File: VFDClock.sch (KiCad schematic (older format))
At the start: 24 parts, among them J1 Barrel_Jack_MountingPin, P1 Power, P2 Analog, P3 Digital, P4 Digital, Q1 VFD_LD8035E, Q2 VFD_LD8035E, Q3 VFD_LD8035E, Q4 VFD_LD8035E, Q5 VFD_LD8035E, Q6 VFD_LD8035E, U1 IC_HT16K33, U2 RTC_DS3231, U3 TBD62783APG, U4 TBD62783APG

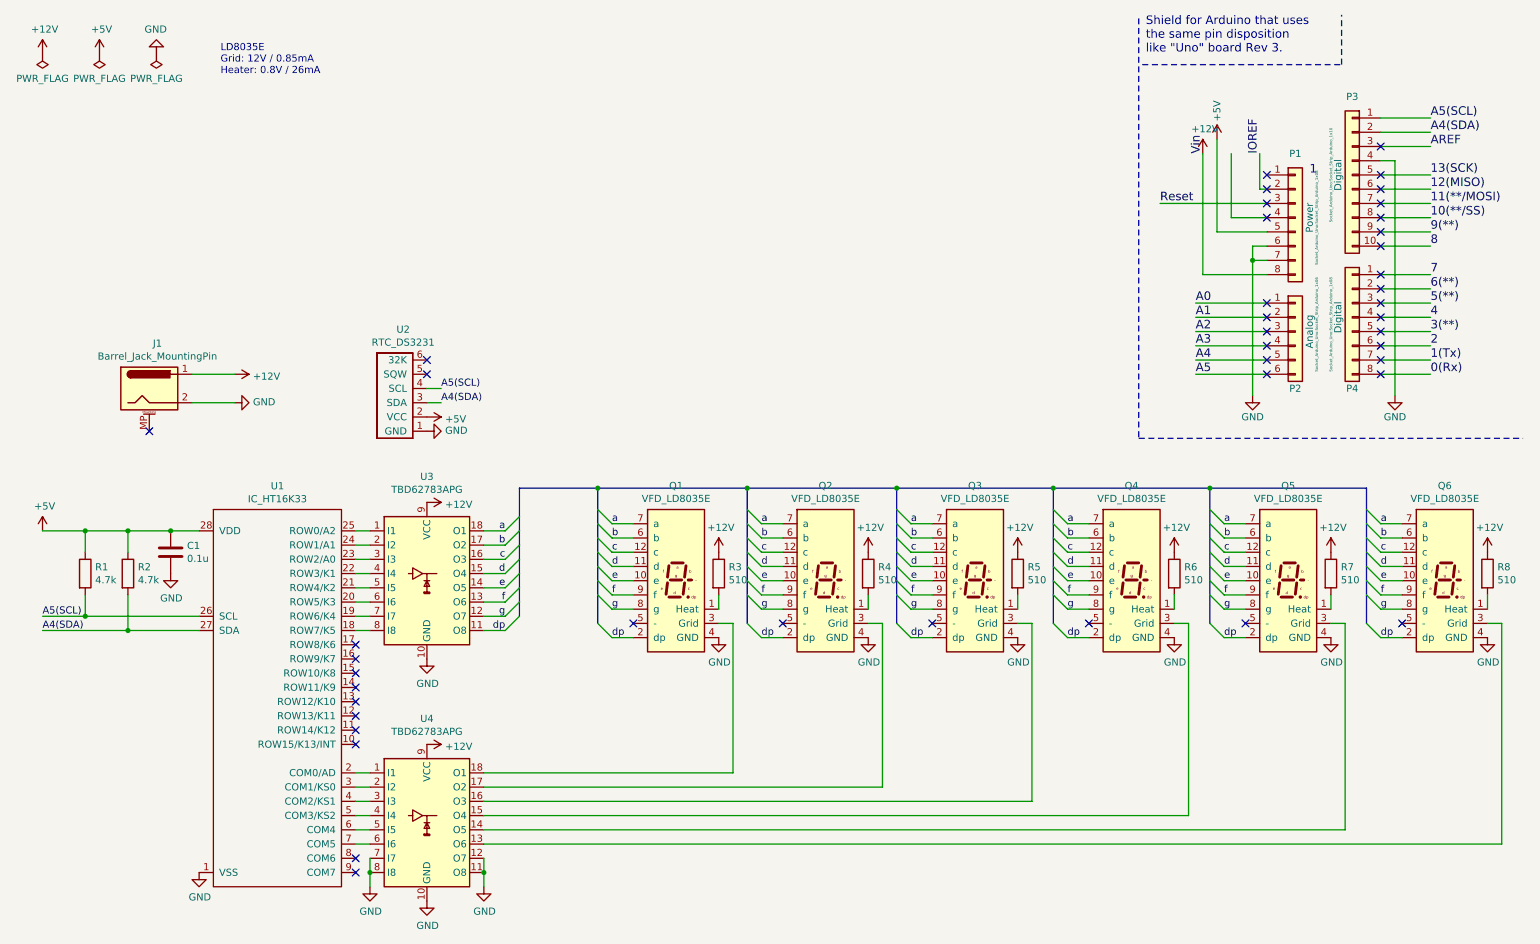
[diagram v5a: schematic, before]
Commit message: RTCを置き換え
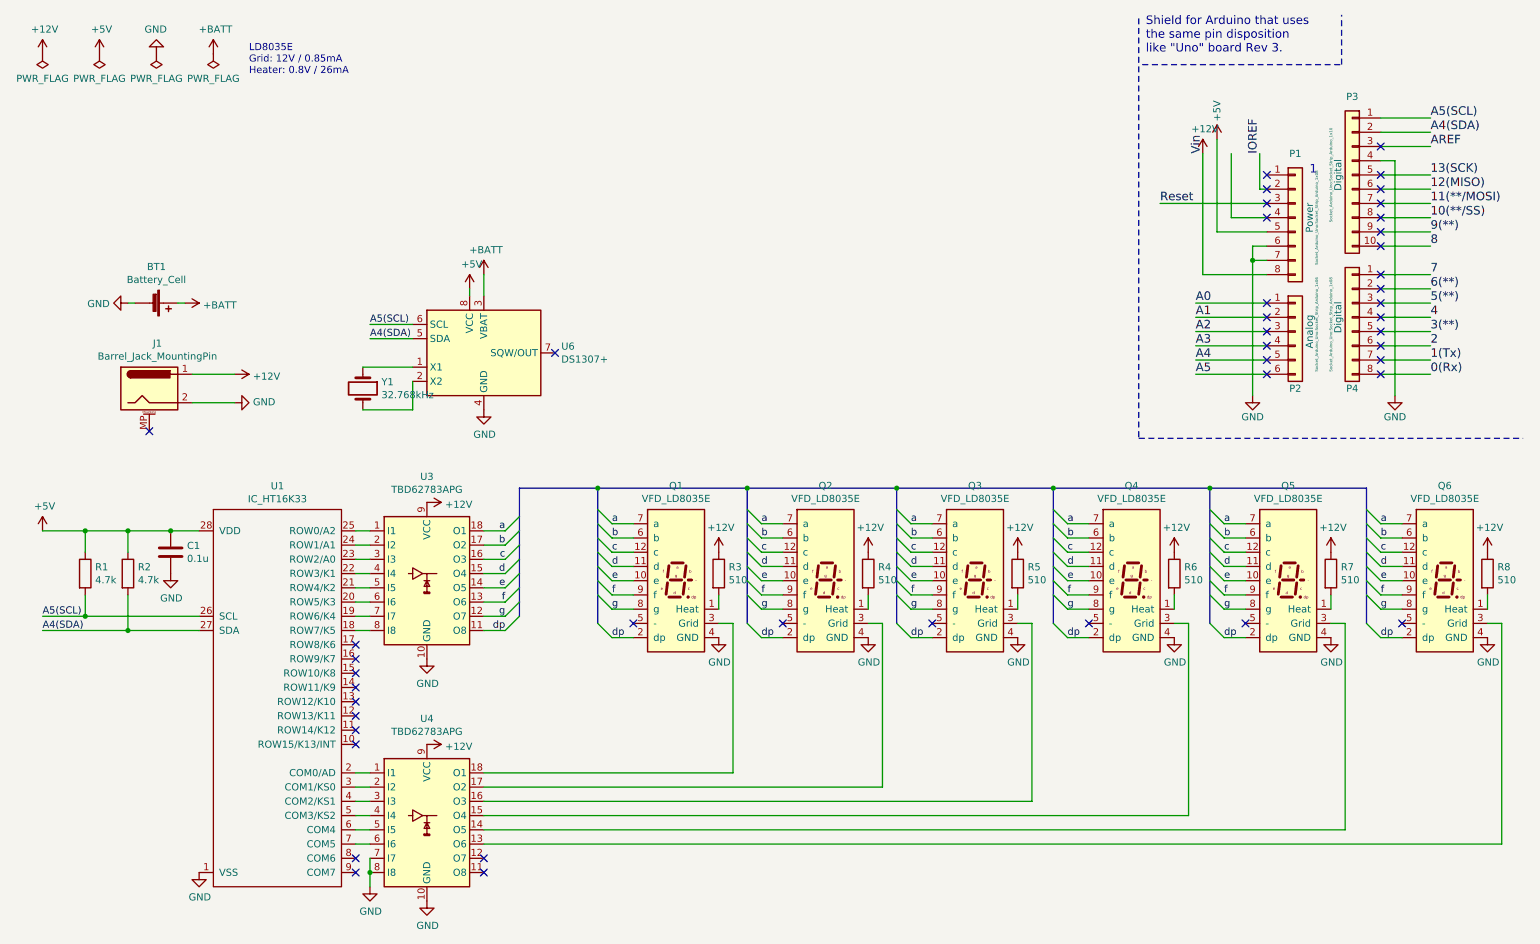
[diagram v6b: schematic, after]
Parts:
- removed U2: RTC_DS3231, #MyFootPrints:RTC_DS3231_Vertical, symbol MyParts:RTC_DS3231
- added BT1: Battery_Cell, symbol Device:Battery_Cell
- added U6: DS1307+, Package_DIP:DIP-8_W7.62mm, symbol Timer_RTC:DS1307+
- added Y1: 32.768kHz, symbol Device:Crystal
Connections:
- net +5V: now also U6.8 (VCC)
- net A4(SDA): now also U6.5 (SDA)
- net A5(SCL): now also U6.6 (SCL)
- net GND: now also BT1.2 (-), U6.4 (GND); no longer U4.11 (O8), U4.12 (O7)
- new net: U6.1 (X1), Y1.1
- new net: U6.2 (X2), Y1.2
- new net +BATT: BT1.1 (+), U6.3 (VBAT)
- no-connect marks 44 -> 45
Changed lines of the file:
@@
 NoConn ~ 9400 3000
-$Comp
-L MyParts:RTC_DS3231 U2
-U 1 1 5F2CBB77
-P 3350 3150
-F 0 "U2" V 3815 3167 50  0000 C CNN
-F 1 "RTC_DS3231" V 3724 3167 50  0000 C CNN
-F 2 "#MyFootPrints:RTC_DS3231_Vertical" H 3350 3500 50  0001 C CNN
-F 3 "" H 3350 3500 50  0001 C CNN
-	1    3350 3150
-	0    -1   -1   0
-$EndComp
-$Comp
-L power:GND #PWR0117
-U 1 1 5F2CDC62
-P 3500 3400
-F 0 "#PWR0117" H 3500 3150 50  0001 C CNN
-F 1 "GND" V 3505 3272 50  0000 R CNN
-F 2 "" H 3500 3400 50  0001 C CNN
-F 3 "" H 3500 3400 50  0001 C CNN
-	1    3500 3400
-	0    -1   -1   0
-$EndComp
-$Comp
-L power:+5V #PWR0118
-U 1 1 5F2CEAC2
-P 3500 3300
-F 0 "#PWR0118" H 3500 3150 50  0001 C CNN
-F 1 "+5V" V 3515 3428 50  0000 L CNN
-F 2 "" H 3500 3300 50  0001 C CNN
-F 3 "" H 3500 3300 50  0001 C CNN
-	1    3500 3300
-	0    1    1    0
-$EndComp
-Wire Wire Line
-	3500 3200 3600 3200
-Wire Wire Line
-	3500 3100 3600 3100
-NoConn ~ 3500 3000
-NoConn ~ 3500 2900
-Text Label 3600 3200 0    50   ~ 0
-A4(SDA)
-Text Label 3600 3100 0    50   ~ 0
-A5(SCL)
 $Comp
 L Transistor_Array:TBD62783A U3
@@
 	0    1    1    0
 $EndComp
-Text Notes 2050 900  0    50   ~ 0
+Text Notes 2250 900  0    50   ~ 0
 LD8035E\nGrid: 12V / 0.85mA\nHeater: 0.8V / 26mA
 $Comp
@@
 $EndComp
 $Comp
-L power:GND #PWR?
+L power:GND #PWR0121
 U 1 1 5F215EAA
 P 3100 6600
-F 0 "#PWR?" H 3100 6350 50  0001 C CNN
+F 0 "#PWR0121" H 3100 6350 50  0001 C CNN
 F 1 "GND" H 3105 6427 50  0000 C CNN
 F 2 "" H 3100 6600 50  0001 C CNN
@@
 	3100 6500 3100 6600
 $Comp
-L power:GND #PWR?
-U 1 1 5F22AE7A
-P 3900 6600
-F 0 "#PWR?" H 3900 6350 50  0001 C CNN
-F 1 "GND" H 3905 6427 50  0000 C CNN
-F 2 "" H 3900 6600 50  0001 C CNN
-F 3 "" H 3900 6600 50  0001 C CNN
-	1    3900 6600
-	1    0    0    -1
-$EndComp
-Wire Wire Line
-	3900 6400 3900 6500
+L Timer_RTC:DS1307+ U6
+U 1 1 5F21DE88
+P 3900 2850
+F 0 "U6" H 4444 2896 50  0000 L CNN
+F 1 "DS1307+" H 4444 2805 50  0000 L CNN
+F 2 "Package_DIP:DIP-8_W7.62mm" H 3900 2350 50  0001 C CNN
+F 3 "https://datasheets.maximintegrated.com/en/ds/DS1307.pdf" H 3900 2650 50  0001 C CNN
+	1    3900 2850
+	1    0    0    -1
+$EndComp
+$Comp
+L power:GND #PWR0117
+U 1 1 5F252546
+P 3900 3250
+F 0 "#PWR0117" H 3900 3000 50  0001 C CNN
+F 1 "GND" H 3905 3077 50  0000 C CNN
+F 2 "" H 3900 3250 50  0001 C CNN
+F 3 "" H 3900 3250 50  0001 C CNN
+	1    3900 3250
+	1    0    0    -1
+$EndComp
+Wire Wire Line
+	3400 2650 3100 2650
+Wire Wire Line
+	3400 2750 3100 2750
+Text Label 3100 2650 0    50   ~ 0
+A5(SCL)
+Text Label 3100 2750 0    50   ~ 0
+A4(SDA)
+$Comp
+L power:+BATT #PWR0118
+U 1 1 5F273890
+P 3900 2300
+F 0 "#PWR0118" H 3900 2150 50  0001 C CNN
+F 1 "+BATT" H 3915 2473 50  0000 C CNN
+F 2 "" H 3900 2300 50  0001 C CNN
+F 3 "" H 3900 2300 50  0001 C CNN
+	1    3900 2300
+	1    0    0    -1
+$EndComp
+Wire Wire Line
+	3900 2300 3900 2450
+Wire Wire Line
+	3800 2400 3800 2450
+$Comp
+L Device:Crystal Y1
+U 1 1 5F293E6C
+P 3050 3100
+F 0 "Y1" V 3004 3231 50  0000 L CNN
+F 1 "32.768kHz" V 3095 3231 50  0000 L CNN
+F 2 "" H 3050 3100 50  0001 C CNN
+F 3 "~" H 3050 3100 50  0001 C CNN
+	1    3050 3100
+	0    1    1    0
+$EndComp
+Wire Wire Line
+	3050 2950 3400 2950
+Wire Wire Line
+	3400 3050 3400 3250
+Wire Wire Line
+	3400 3250 3050 3250
+$Comp
+L power:PWR_FLAG #FLG0103
+U 1 1 5F2B7A6D
+P 2000 750
+F 0 "#FLG0103" H 2000 825 50  0001 C CNN
+F 1 "PWR_FLAG" H 2000 923 50  0000 C CNN
+F 2 "" H 2000 750 50  0001 C CNN
+F 3 "~" H 2000 750 50  0001 C CNN
+	1    2000 750
+	-1   0    0    1
+$EndComp
+$Comp
+L power:+BATT #PWR0124
+U 1 1 5F2D6E5F
+P 2000 750
+F 0 "#PWR0124" H 2000 600 50  0001 C CNN
+F 1 "+BATT" H 2015 923 50  0000 C CNN
+F 2 "" H 2000 750 50  0001 C CNN
+F 3 "" H 2000 750 50  0001 C CNN
+	1    2000 750
+	1    0    0    -1
+$EndComp
+$Comp
+L power:+5V #PWR0123
+U 1 1 5F2E22E1
+P 3800 2400
+F 0 "#PWR0123" H 3800 2250 50  0001 C CNN
+F 1 "+5V" H 3815 2573 50  0000 C CNN
+F 2 "" H 3800 2400 50  0001 C CNN
+F 3 "" H 3800 2400 50  0001 C CNN
+	1    3800 2400
+	1    0    0    -1
+$EndComp
+NoConn ~ 4400 2850
+NoConn ~ 3900 6400
+NoConn ~ 3900 6500
+$Comp
+L Device:Battery_Cell BT1
+U 1 1 5F30F794
+P 1550 2500
+F 0 "BT1" V 1295 2550 50  0000 C CNN
+F 1 "Battery_Cell" V 1386 2550 50  0000 C CNN
+F 2 "" V 1550 2560 50  0001 C CNN
+F 3 "~" V 1550 2560 50  0001 C CNN
+	1    1550 2500
+	0    1    1    0
+$EndComp
+Wire Wire Line
+	1450 2500 1400 2500
+$Comp
+L power:GND #PWR0122
+U 1 1 5F3335A2
+P 1400 2500
+F 0 "#PWR0122" H 1400 2250 50  0001 C CNN
+F 1 "GND" V 1405 2372 50  0000 R CNN
+F 2 "" H 1400 2500 50  0001 C CNN
+F 3 "" H 1400 2500 50  0001 C CNN
+	1    1400 2500
+	0    1    1    0
+$EndComp
+$Comp
+L power:+BATT #PWR0125
+U 1 1 5F332ED0
+P 1800 2500
+F 0 "#PWR0125" H 1800 2350 50  0001 C CNN
+F 1 "+BATT" V 1815 2628 50  0000 L CNN
+F 2 "" H 1800 2500 50  0001 C CNN
+F 3 "" H 1800 2500 50  0001 C CNN
+	1    1800 2500
+	0    1    1    0
+$EndComp
+Wire Wire Line
+	1800 2500 1750 2500
 Wire Bus Line
 	10100 3800 10100 4750
@@
 Wire Bus Line
 	4700 3800 4700 4750
-Connection ~ 3900 6500
-Wire Wire Line
-	3900 6500 3900 6600
 $EndSCHEMATC

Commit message: 部品を仮配置
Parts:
- BT1: footprint (none) -> #MyFootPrints:Battery_CR2032_CH74-2032LF
- Y1: footprint (none) -> Crystal:Crystal_DS26_D2.0mm_L6.0mm_Vertical
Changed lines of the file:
@@
 F 0 "Y1" V 3004 3231 50  0000 L CNN
 F 1 "32.768kHz" V 3095 3231 50  0000 L CNN
-F 2 "" H 3050 3100 50  0001 C CNN
+F 2 "Crystal:Crystal_DS26_D2.0mm_L6.0mm_Vertical" H 3050 3100 50  0001 C CNN
 F 3 "~" H 3050 3100 50  0001 C CNN
 	1    3050 3100
@@
 F 0 "BT1" V 1295 2550 50  0000 C CNN
 F 1 "Battery_Cell" V 1386 2550 50  0000 C CNN
-F 2 "" V 1550 2560 50  0001 C CNN
+F 2 "#MyFootPrints:Battery_CR2032_CH74-2032LF" V 1550 2560 50  0001 C CNN
 F 3 "~" V 1550 2560 50  0001 C CNN
 	1    1550 2500
